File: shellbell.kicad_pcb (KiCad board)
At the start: 2 copper layers, 42.5 x 24.5 mm, 23 parts, among them J1 Barrel_Jack_MountingPin, J2 Conn_02x04_Odd_Even, J3 USB_B_Mini, Q1 IRLB8721PBF, U1 LD1117V33, U2 FT230XS-U

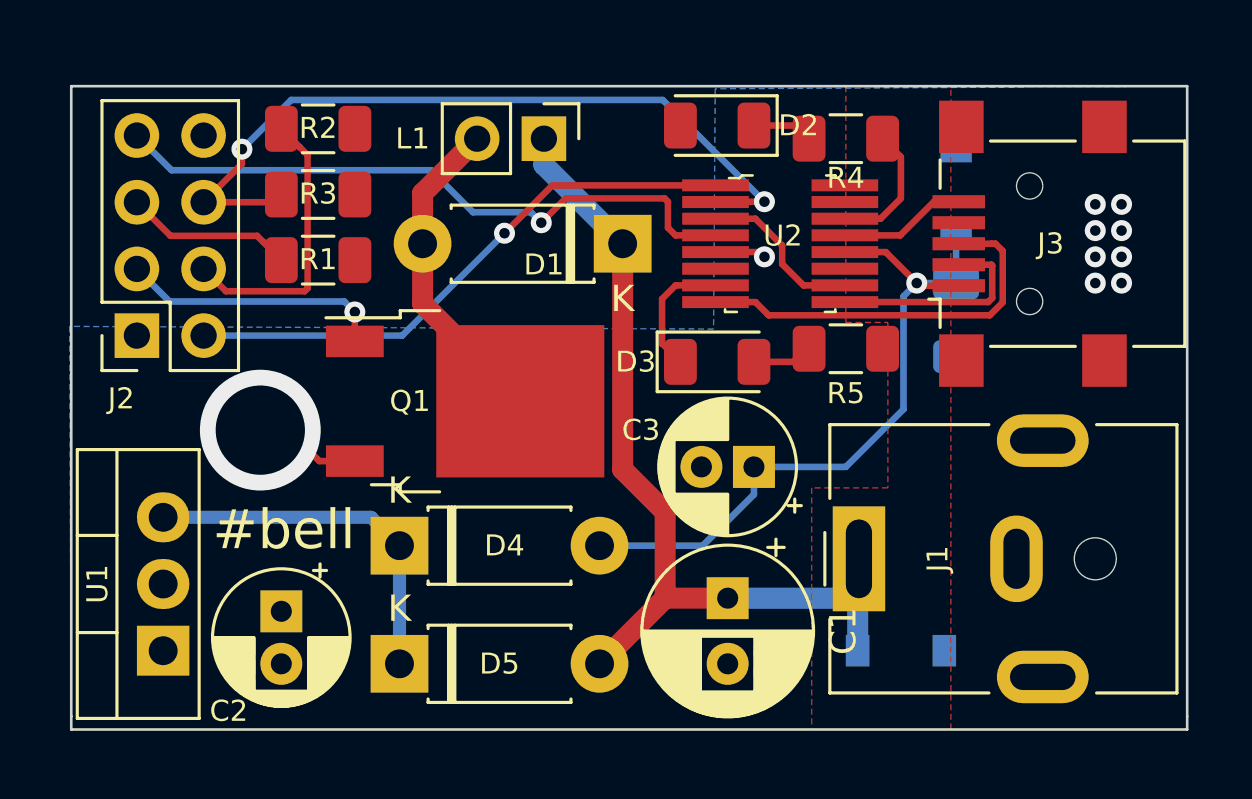
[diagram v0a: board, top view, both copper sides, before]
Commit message: Fixes TX/RX. Removes RTS-reset. Clean up.
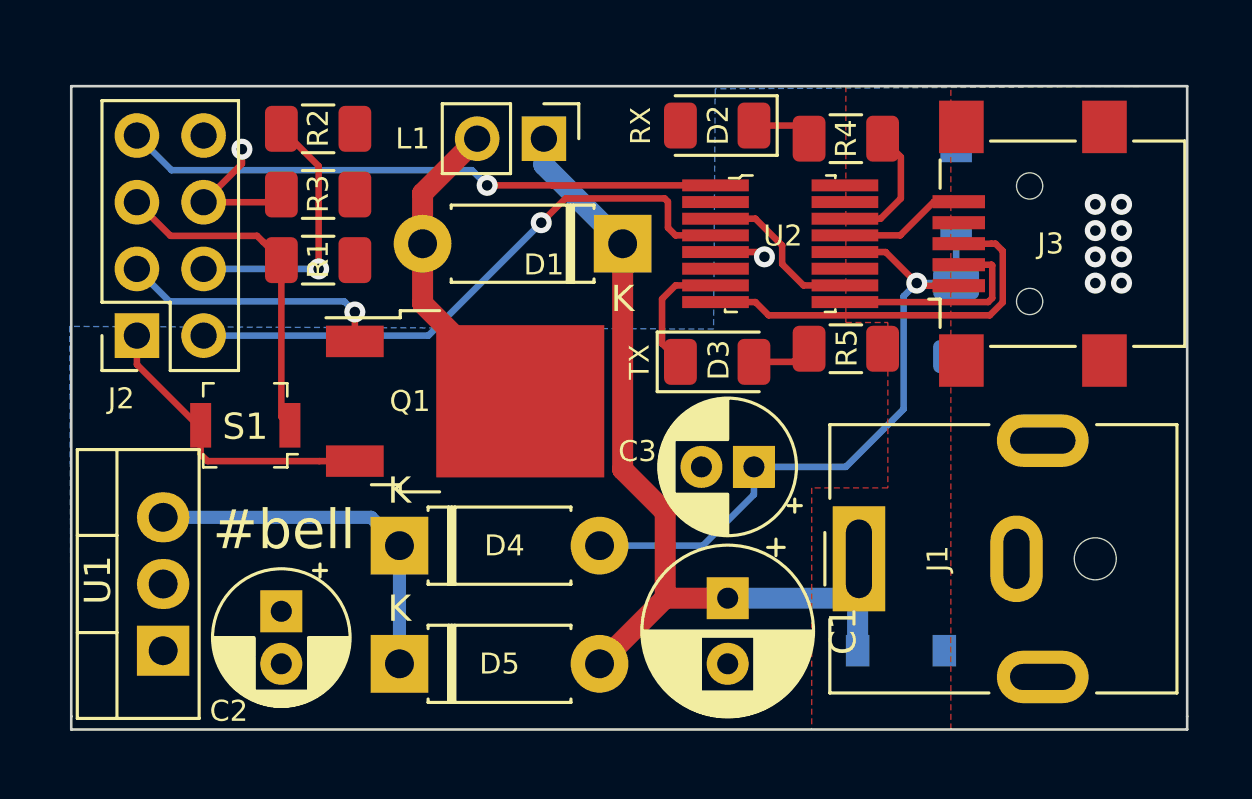
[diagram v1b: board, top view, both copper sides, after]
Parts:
- added S1: B3U-1000P, digikey-footprints:Switch_Tactile_SMD_B3U-1000P, F.Cu at (136.6, 107.4)
- D1: value DIODE -> D
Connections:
- net Net-(D1-Pad2) renamed /LGND
- net Net-(D3-Pad1) renamed /TX_LED#
- net Net-(J2-Pad3) renamed /CTL
- net Net-(J2-Pad4) renamed /CH_PD
- net Net-(J2-Pad5) renamed /GPIO0
- net Net-(J3-Pad2) renamed /USBDM
- net Net-(J3-Pad3) renamed /USBDP
- net Net-(R4-Pad1) renamed /RX_LED#
- net Net-(U2-Pad10) renamed /VCCIO
- J2 pad 2: Net-(J2-Pad2) -> /RXD
- J2 pad 6: Net-(J2-Pad6) -> /RST
- J2 pad 7: Net-(J2-Pad7) -> /TXD
- R3 pad 2: Net-(J2-Pad6) -> /RST
- U2 pad 1: Net-(J2-Pad2) -> /TXD
- U2 pad 2: Net-(J2-Pad6) -> Net-(U2-Pad2)
- U2 pad 4: Net-(J2-Pad7) -> /RXD
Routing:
- net Net-(J2-Pad6): track 29.9 -> 0.00 mm, vias 2 -> 0
- net Net-(J2-Pad7): track 25.0 -> 0.00 mm, vias 1 -> 0
- net /RXD: track 0.00 -> 22.8 mm, vias 0 -> 1
- net /TXD: track 0.00 -> 22.8 mm, vias 0 -> 1
- net Net-(J2-Pad2): track 21.9 -> 0.00 mm, vias 1 -> 0
- net GND: track 11.5 -> 19.0 mm, vias 10 -> 9
- net /GPIO0: track 6.42 -> 12.8 mm
- net /RST: track 0.00 -> 5.71 mm, vias 0 -> 1
- net /CH_PD: track 10.8 -> 10.3 mm, vias 0 -> 1
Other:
- board text added: "RX"
- board text added: "TX"

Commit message: Add programming buttons and rerouting.
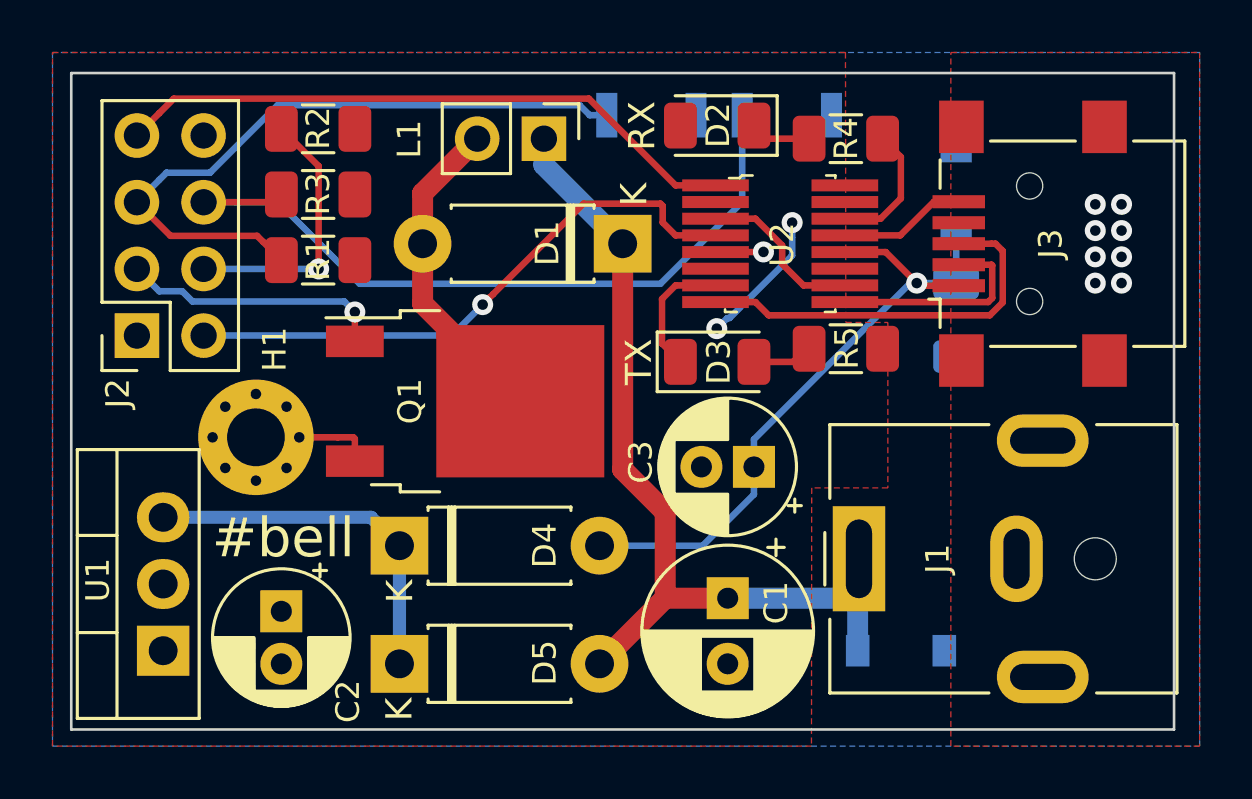
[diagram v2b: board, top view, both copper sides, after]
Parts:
- removed S1: B3U-1000P, digikey-footprints:Switch_Tactile_SMD_B3U-1000P
- added H1: MountingHole_Pad, MountingHole:MountingHole_2.2mm_M2_Pad_Via, F.Cu at (137.0, 107.9)
- added S2: GPIO0, B3U-3000P:SW_B3U-3000P, B.Cu at (152.1, 95.6)
- added S3: RST, B3U-3000P:SW_B3U-3000P, B.Cu at (157.3, 95.6)
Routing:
- net /RST: track 5.71 -> 29.5 mm, vias 1 -> 0
- net /GPIO0: track 12.8 -> 26.0 mm
- net GND: track 19.0 -> 13.3 mm
- net +3V3: track 0.00 -> 5.27 mm, vias 0 -> 2
- net +5V: track 27.5 -> 25.6 mm
- net /TXD: track 22.8 -> 24.0 mm, vias 1 -> 0
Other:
- board size 42.5 x 24.5 mm -> 42 x 25 mm
